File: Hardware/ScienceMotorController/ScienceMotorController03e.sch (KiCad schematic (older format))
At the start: 17 parts, among them U6 VNH5019A_E

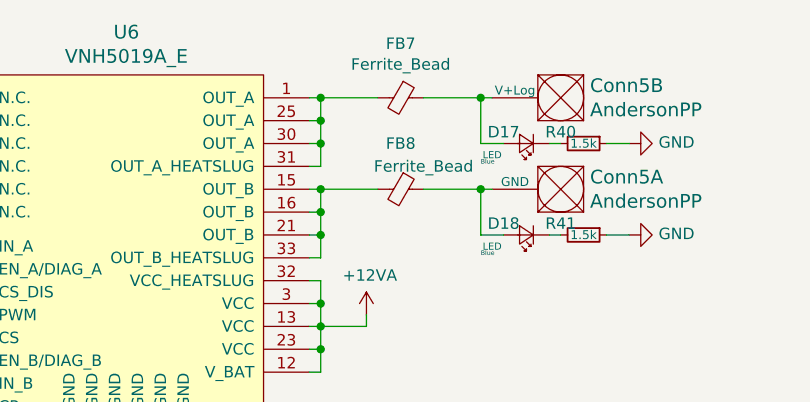
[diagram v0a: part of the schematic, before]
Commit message: finished assigning footprints, generated pcbnew
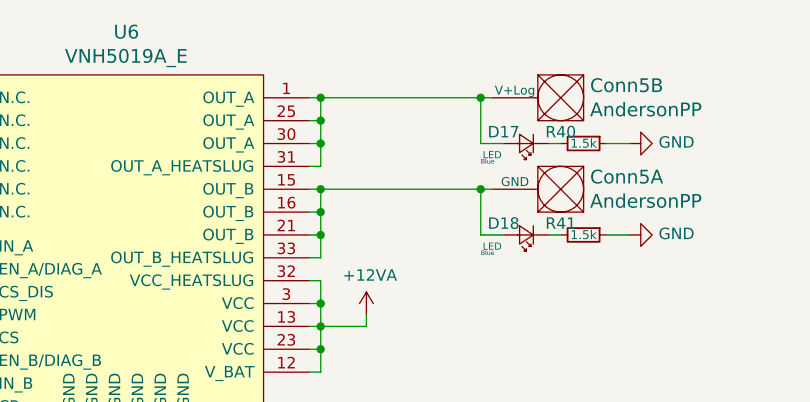
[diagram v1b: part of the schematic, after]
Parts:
- removed FB7, FB8: Ferrite_Bead, symbol Device:Ferrite_Bead_Small
- Conn5: footprint MRDT_Connectors:Anderson_2_Vertical_Sidy_by_Side -> MRDT_Connectors:Anderson_2_Horizontal_Side_by_Side
- U6: footprint (none) -> MRDT_ICs:MultiPowerSO_30
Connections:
- net at Conn5.2 (V+Log), D17.2 (A): now also U6.1 (OUT_A), U6.25 (OUT_A), U6.30 (OUT_A), U6.31 (OUT_A_HEATSLUG)
- net at Conn5.1 (GND), D18.2 (A): now also U6.15 (OUT_B), U6.16 (OUT_B), U6.21 (OUT_B), U6.33 (OUT_B_HEATSLUG)
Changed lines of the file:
@@
 F 0 "U6" H 5500 6037 60  0000 C CNN
 F 1 "VNH5019A_E" H 5500 5931 60  0000 C CNN
-F 2 "" H 4900 5650 60  0001 C CNN
+F 2 "MRDT_ICs:MultiPowerSO_30" H 4900 5650 60  0001 C CNN
 F 3 "" H 4900 5650 60  0001 C CNN
 	1    4900 4350
@@
 F 0 "Conn5" H 7472 3297 60  0000 R CNN
 F 1 "AndersonPP" H 7472 3403 60  0000 R CNN
-F 2 "MRDT_Connectors:Anderson_2_Vertical_Sidy_by_Side" H 7350 2700 60  0001 C CNN
+F 2 "MRDT_Connectors:Anderson_2_Horizontal_Side_by_Side" H 7350 2700 60  0001 C CNN
 F 3 "" H 7350 2700 60  0001 C CNN
 	1    7500 3250
@@
 F 0 "Conn5" H 7472 2897 60  0000 R CNN
 F 1 "AndersonPP" H 7472 3003 60  0000 R CNN
-F 2 "MRDT_Connectors:Anderson_2_Vertical_Sidy_by_Side" H 7350 2300 60  0001 C CNN
+F 2 "MRDT_Connectors:Anderson_2_Horizontal_Side_by_Side" H 7350 2300 60  0001 C CNN
 F 3 "" H 7350 2300 60  0001 C CNN
 	2    7500 2850
@@
 	4700 4000 3750 4000
 Connection ~ 3750 4000
-Wire Wire Line
-	6800 2950 7050 2950
-Wire Wire Line
-	6800 3350 7050 3350
 Wire Wire Line
 	7050 3150 7050 2950
@@
 	1    0    0    -1
 $EndComp
-$Comp
-L Device:Ferrite_Bead_Small FB?
-U 1 1 5F9F76C5
-P 6700 2950
-AR Path="/5F9082FE/5F9F76C5" Ref="FB?"  Part="1"
-AR Path="/5F7148FA/5FA34ADB/5F9F76C5" Ref="FB7"  Part="1"
-F 0 "FB7" V 6463 2950 50  0000 C CNN
-F 1 "Ferrite_Bead" V 6554 2950 50  0000 C CNN
-F 2 "" V 6630 2950 50  0001 C CNN
-F 3 "~" H 6700 2950 50  0001 C CNN
-	1    6700 2950
-	0    1    1    0
-$EndComp
-$Comp
-L Device:Ferrite_Bead_Small FB?
-U 1 1 5F9F8032
-P 6700 3350
-AR Path="/5F9082FE/5F9F8032" Ref="FB?"  Part="1"
-AR Path="/5F7148FA/5FA34ADB/5F9F8032" Ref="FB8"  Part="1"
-F 0 "FB8" V 6500 3350 50  0000 C CNN
-F 1 "Ferrite_Bead" V 6600 3450 50  0000 C CNN
-F 2 "" V 6630 3350 50  0001 C CNN
-F 3 "~" H 6700 3350 50  0001 C CNN
-	1    6700 3350
-	0    1    1    0
-$EndComp
-Wire Wire Line
-	6600 2950 6350 2950
 Connection ~ 6350 2950
-Wire Wire Line
-	6600 3350 6350 3350
 Connection ~ 6350 3350
 Text HLabel 4250 3600 0    50   Input ~ 0
@@
 Text Notes 7050 3250 0    20   ~ 0
 Blue
+Wire Wire Line
+	6350 3350 7050 3350
+Wire Wire Line
+	6350 2950 7050 2950
 $EndSCHEMATC

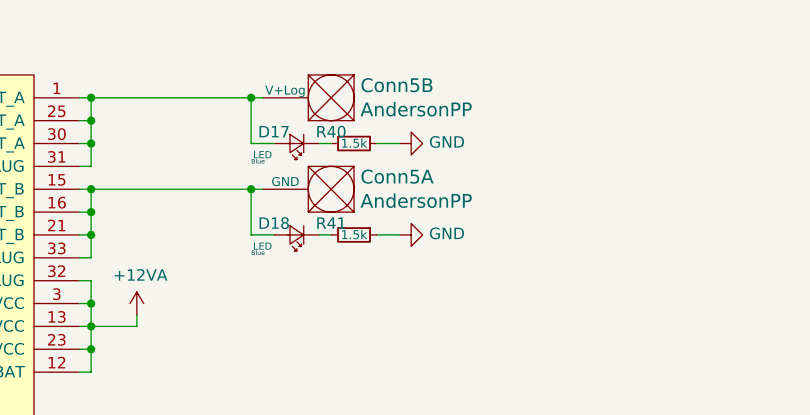
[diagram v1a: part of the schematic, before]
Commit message: running traces
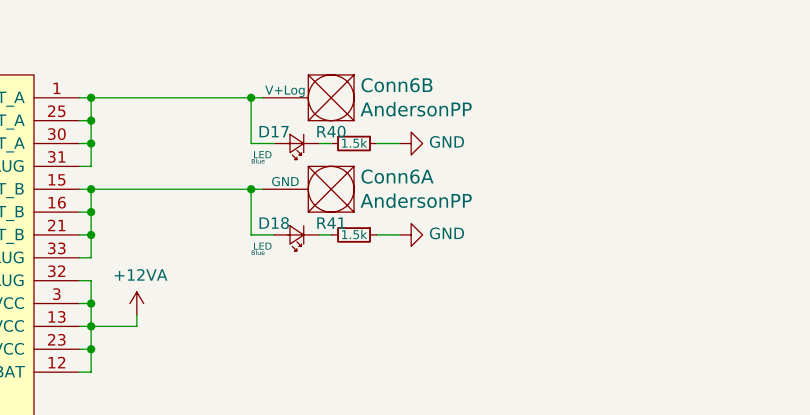
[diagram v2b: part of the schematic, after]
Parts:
- renumbered Conn5 to Conn6
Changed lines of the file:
@@
 AR Path="/5F7D111E/5FA666AF/5FAB3680" Ref="Conn?"  Part="1"
 AR Path="/5F9082FE/5FAB3680" Ref="Conn?"  Part="1"
-AR Path="/5F7148FA/5FA34ADB/5FAB3680" Ref="Conn5"  Part="1"
-F 0 "Conn5" H 7472 3297 60  0000 R CNN
+AR Path="/5F7148FA/5FA34ADB/5FAB3680" Ref="Conn6"  Part="1"
+F 0 "Conn6" H 7472 3297 60  0000 R CNN
 F 1 "AndersonPP" H 7472 3403 60  0000 R CNN
 F 2 "MRDT_Connectors:Anderson_2_Horizontal_Side_by_Side" H 7350 2700 60  0001 C CNN
@@
 AR Path="/5F7D111E/5FA666AF/5FAB3686" Ref="Conn?"  Part="2"
 AR Path="/5F9082FE/5FAB3686" Ref="Conn?"  Part="2"
-AR Path="/5F7148FA/5FA34ADB/5FAB3686" Ref="Conn5"  Part="2"
-F 0 "Conn5" H 7472 2897 60  0000 R CNN
+AR Path="/5F7148FA/5FA34ADB/5FAB3686" Ref="Conn6"  Part="2"
+F 0 "Conn6" H 7472 2897 60  0000 R CNN
 F 1 "AndersonPP" H 7472 3003 60  0000 R CNN
 F 2 "MRDT_Connectors:Anderson_2_Horizontal_Side_by_Side" H 7350 2300 60  0001 C CNN
